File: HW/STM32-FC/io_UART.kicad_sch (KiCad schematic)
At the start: 2 parts, among them J10 Conn_01x06, J11 Conn_01x06

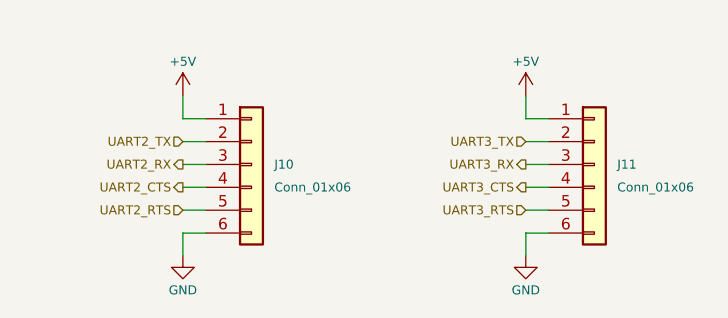
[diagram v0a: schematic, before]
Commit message: RC IN modified
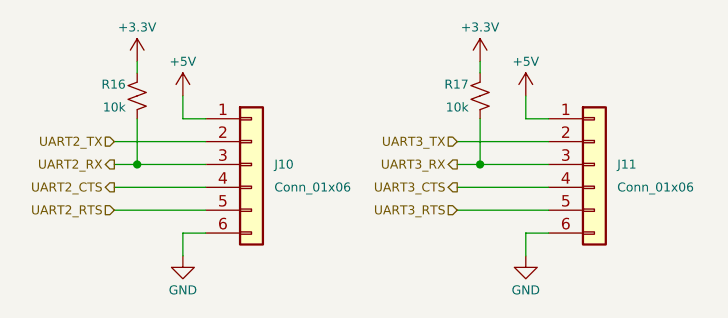
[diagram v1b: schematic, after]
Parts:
- added R16, R17: 10k, Resistor_SMD:R_0402_1005Metric, symbol Device:R_Small_US
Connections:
- net UART2_RX: now also R16.2
- net UART3_RX: now also R17.2
- new net +3.3V: R16.1, R17.1
